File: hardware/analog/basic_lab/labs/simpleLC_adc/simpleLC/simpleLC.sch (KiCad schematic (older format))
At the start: 0 parts

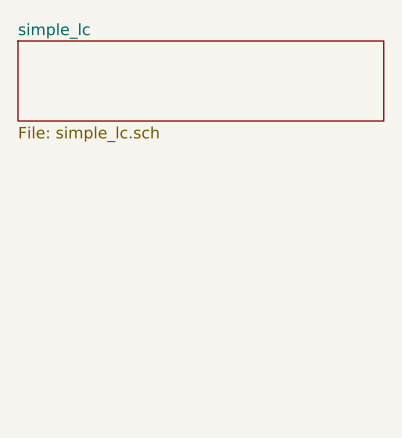
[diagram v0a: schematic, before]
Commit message: pwm => adc: started amplifier PCB
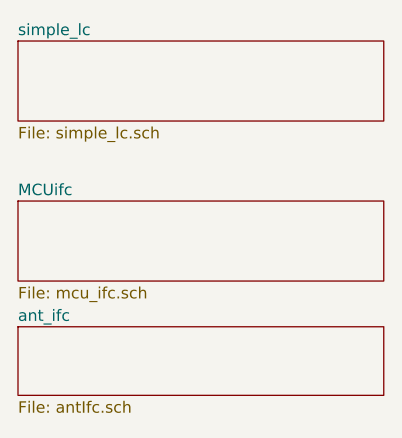
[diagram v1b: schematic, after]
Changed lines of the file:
@@
 $Descr A4 11693 8268
 encoding utf-8
-Sheet 1 2
+Sheet 1 4
 Title ""
 Date ""
@@
 F1 "simple_lc.sch" 50
 $EndSheet
+$Sheet
+S 2250 3400 1600 350
+U 60F86F5B
+F0 "MCUifc" 50
+F1 "mcu_ifc.sch" 50
+$EndSheet
+$Sheet
+S 2250 3950 1600 300
+U 60F87023
+F0 "ant_ifc" 50
+F1 "antIfc.sch" 50
+$EndSheet
 $EndSCHEMATC
